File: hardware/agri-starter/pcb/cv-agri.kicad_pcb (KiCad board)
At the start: 2 copper layers, 110.2 x 87.3 mm, 54 parts, among them J1 2P 5.08mm, J2 2P 5.08mm, J3 4P 5.08mm, K1 SRD-05VDC-SL-C, M1 SIM800L, Q1 S8050, U1 ESP32-WROOM-32E (4MB), U2 AMS1117-3.3, U3 MP1584 buck (4V)

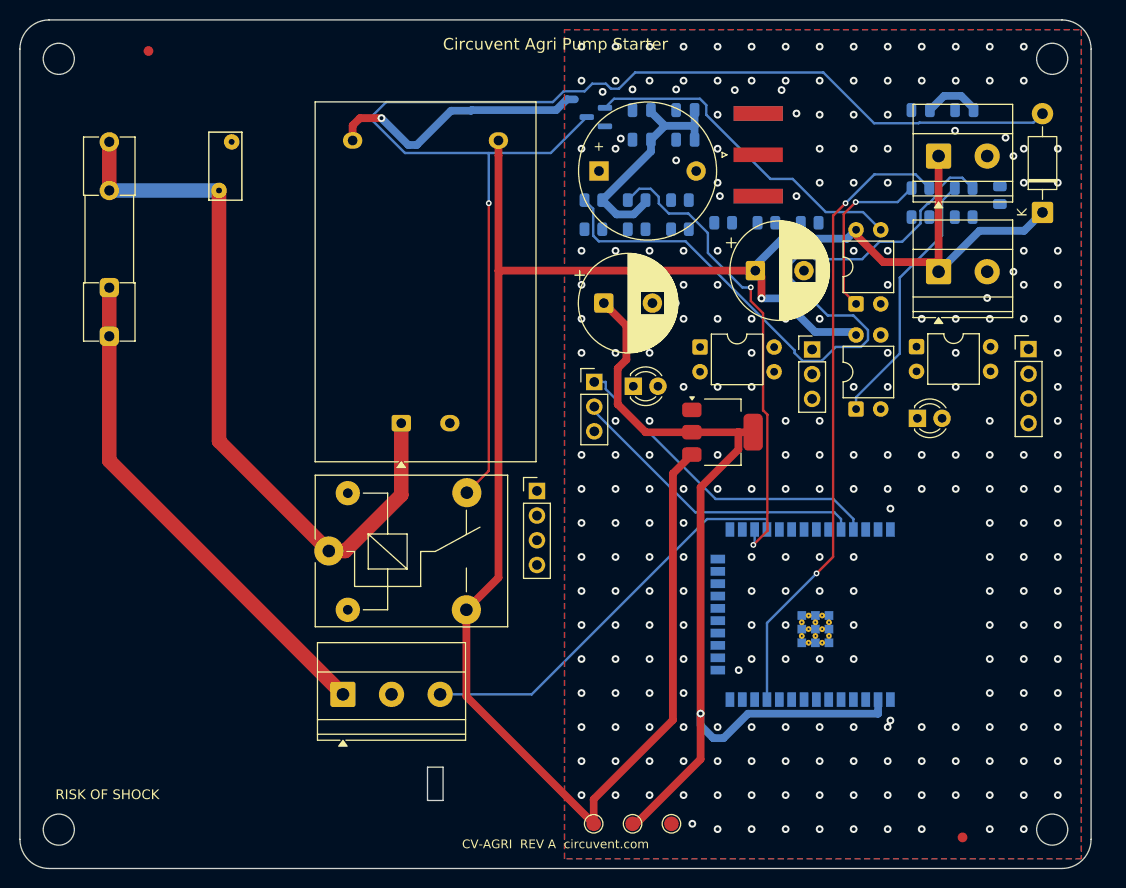
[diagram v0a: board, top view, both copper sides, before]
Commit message: hardware: fix mains isolation barrier gaps, add load-controller PCB
Adds the 13th board (ultra-compact dual-channel load controller: ESP32-C3,
opto+relay channel, MOSFET PWM channel, USB-C, AP2112K LDO, USBLC6 ESD) and
regenerates all 12 existing boards, which were stale with respect to earlier
relay-pinout and LED-polarity fixes.

The substantive change is to the mains isolation barrier. It is a keepout band
the router must not cross, deliberately cut where a component straddles it
because there the isolation is provided by the part's package. Three linked
defects made those cuts unsafe, each only visible once the previous was fixed:

1. The cut removed the barrier across the full band width for the straddling
   part's whole height, while the ISO_BRIDGE area that excuses the gap covered
   only the part itself. The router used the leftover strip beside the part to
   bring +5V within 6.99 mm of AC_N against an 8.0 mm reinforced creepage rule.
2. Straddling parts can overlap in y, so cutting per part put one part's
   keepout on another part's pads. The exempt x-ranges are now unioned per
   strip by a sweep line.
3. The rule only relaxes for items insideArea('ISO_BRIDGE'). With the hole the
   same size as the area, a track could hug the hole's edge without being
   contained in it, so the rule fired anyway and the router had no way to know.
   The hole is now the part's pad bbox + 0.3 mm, strictly inside ISO_BRIDGE at
   the footprint bbox + 0.6 mm.

The tighter hole leaves mains nets less room to reach bridge pads, so some
boards report more unconnected items. That is deliberate: those are documented
hand-routing items, whereas a creepage violation is a safety defect.

Also fixed in the generator:
- _pad_shape() derived a pad's layers from PAD::GetLayer(), which returns F.Cu
  even for pads on B.Cu. Every back-side pad became a phantom obstacle on the
  front, blocking legal paths there while hiding the real one behind. Only
  IsOnLayer() is truthful.
- Castella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
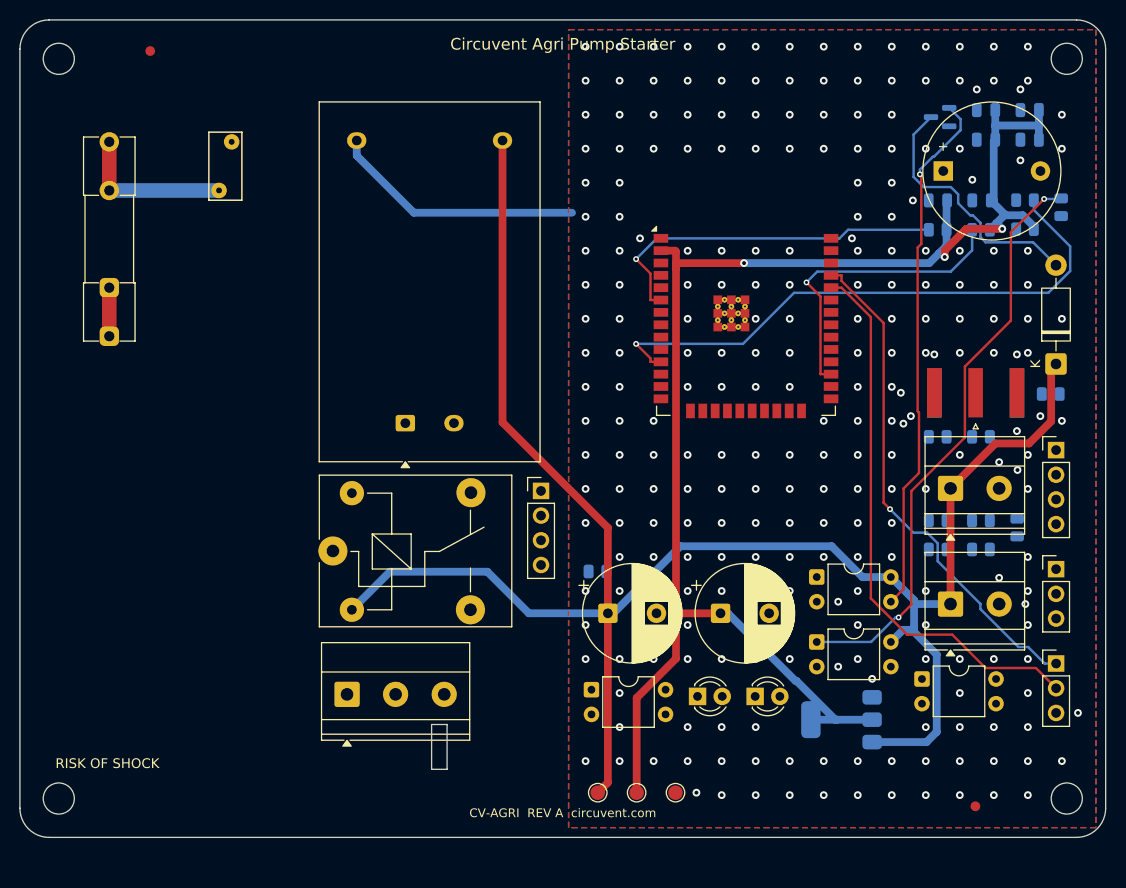
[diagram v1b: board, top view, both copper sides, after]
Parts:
- U1: moved to F.Cu
- U2: moved to B.Cu
- moved JP 55.6 mm to (206.6, 146.2)
- moved R13 48.4 mm to (198.9, 134.5)
- moved R12 48.4 mm to (194.4, 134.5)
- moved R6 43.0 mm to (206.0, 118.5)
- moved C1 38.4 mm to (160.5, 141.0)
- moved R11 37.9 mm to (202.6, 132.2), turned to 90 degrees
- moved R10 37.7 mm to (198.9, 131.5)
- moved R9 37.7 mm to (194.4, 131.5)
- moved PC4 37.0 mm to (158.8, 148.9)
- moved R14 36.2 mm to (159.4, 136.7)
- moved R5 35.6 mm to (198.9, 101.6)
- moved R4 35.6 mm to (194.4, 101.6)
- moved C2 35.4 mm to (199.4, 89.3)
- moved C3 35.4 mm to (203.9, 89.3)
- moved FB1 35.4 mm to (195.0, 95.5)
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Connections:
- K1 pad 2: PUMP_RELAY_SW -> +5V
- K1 pad 3: +5V -> PUMP_RELAY_SW
- K1 pad 4: PUMP_RELAY_COIL -> N$K1.4
- K1 pad 5: N$K1.5 -> PUMP_RELAY_COIL
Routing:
- net PUMP_RELAY_COIL: track 135.0 -> 26.7 mm, vias 1 -> 0
- net AC_L_FUSED: track 75.3 -> 16.3 mm
- net AC_L: track 51.8 -> 5.00 mm
- net SIM_TX: track 42.2 -> 0.00 mm
- net MAINS_SENSE: track 75.6 -> 37.3 mm, vias 0 -> 1
- net MAINS_SENSE_OPT: track 26.9 -> 60.5 mm, vias 0 -> 2
- net +3V3: track 124.6 -> 153.6 mm, vias 1 -> 3
- net UART_RX: track 31.5 -> 57.2 mm
- net PUMP_RELAY_DRV: track 34.9 -> 54.6 mm, vias 0 -> 1
- net UART_TX: track 34.0 -> 52.2 mm, vias 0 -> 1
- net PUMP_RELAY_OPT: track 17.9 -> 0.00 mm, vias 1 -> 0
- net SIM_RX: track 48.4 -> 31.6 mm, vias 2 -> 1
- net +5V: track 207.8 -> 197.8 mm, vias 1 -> 0
- net PUMP_RELAY: track 64.8 -> 60.1 mm, vias 2 -> 1
- net GND: track 27.8 -> 26.1 mm, vias 256 -> 254
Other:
- board size 110.2 x 87.3 mm -> 111.7 x 84.1 mm

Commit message: Release 1.10.0, and stop shipping permissions the app never uses
Cut 1.10.0 (versionCode 12) and built it: AAB 38 MB, APK 83 MB, signed with the
upload key, JS bundle embedded.

Checking the generated manifest before writing the Play listing turned up
permissions no one had asked for. Every one of them is printed on the store page
for users to read before they install:

  RECORD_AUDIO          expo-camera asks for the microphone so video can be
                        recorded with sound. This app only ever puts the camera
                        in barcode mode to read a QR label, and expo-speech is
                        output-only - it speaks, it does not listen. Left in,
                        Play lists "Microphone" against a home-control app,
                        which is alarming, unexplainable and untrue.
  SYSTEM_ALERT_WINDOW   React Native's development overlay, useless in a release
                        build and shown to users as "Display over other apps".
  READ/WRITE_EXTERNAL_STORAGE
                        Legacy storage access nothing here touches.

Stripped via android.blockedPermissions. That emits tools:node="remove", which
is a merge instruction rather than a guarantee, so it was checked against the
finished artifact with aapt2 rather than the source manifest - all four are
absent from the APK.

NEARBY_WIFI_DEVICES now carries neverForLocation. Android otherwise treats it as
location-capable, because knowing which networks are in range is enough to place
someone, and Play's data safety review treats it the same way. The app uses it
only to join a new device's setup hotspot. That flag is a promise, so the plugin
says plainly that it has to come off if scan results are ever used positionally.

What is left is defensible: location for Wi-Fi onboarding (Android requires it),
camera for the QR label, nearby-devices flagged as non-positional.

Added mobile/store/listing with the text Play asks for - title, short and full
descriptions, and what'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
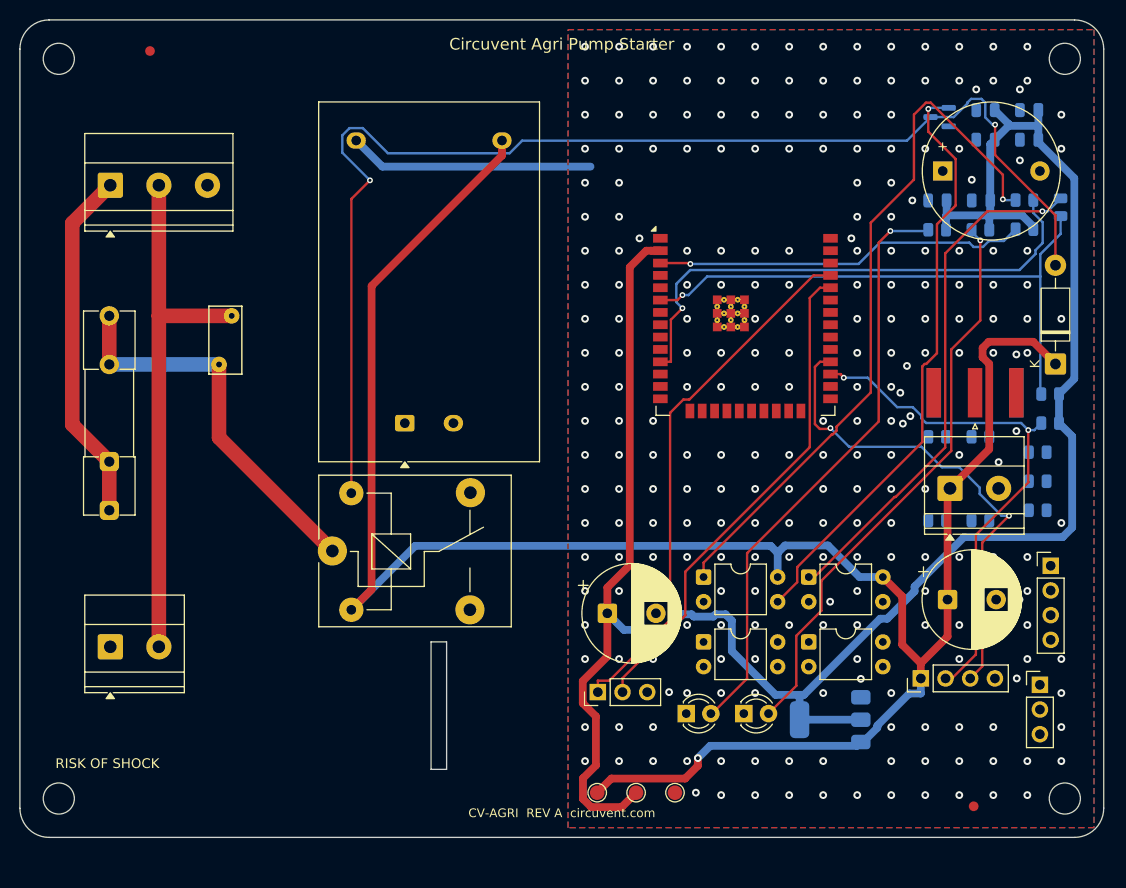
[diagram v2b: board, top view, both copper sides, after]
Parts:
- moved J2 88.0 mm to (109.3, 144.5)
- moved J1 57.8 mm to (109.3, 97.0)
- moved JP 47.2 mm to (159.5, 149.2), turned to 90 degrees
- moved M1 43.6 mm to (192.7, 147.7), turned to 90 degrees
- moved R14 39.7 mm to (198.8, 131.5)
- moved C1 35.0 mm to (195.4, 139.6)
- moved PC4 22.9 mm to (181.2, 144.0)
- moved PC3 22.8 mm to (170.3, 144.0)
- moved F1 17.9 mm to (109.2, 130.4)
- moved RV1 17.9 mm to (120.5, 115.4)
- moved SIM1 12.0 mm to (204.9, 148.4)
- moved U3 11.9 mm to (206.0, 136.2)
- moved J3 11.9 mm to (195.7, 128.2)
- moved R7 11.7 mm to (206.0, 121.5)
- moved Cs 11.6 mm to (160.4, 141.0)
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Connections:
- J1 pad 3: SIM_TX -> PE
- J2 pad 1: +5V -> PUMP_RELAY_SW
- J2 pad 2: GND -> AC_N
- LED0 pad 1: N$LED0.1 -> GND
- LED0 pad 2: N$LED0.2 -> LED0_A
- LED1 pad 1: N$LED1.1 -> GND
- LED1 pad 2: N$LED1.2 -> LED1_A
- M1 pad 2: PUMP_RELAY_SW -> SIM_RX
- M1 pad 3: SIM_RX -> SIM_TX
- M1 pad 4: AC_N -> GND
- R4 pad 2: MAINS_SENSE -> LED0_A
- R5 pad 2: SIM_RX -> LED1_A
- R6 pad 1: N$R6.1 -> +3V3
- R6 pad 2: N$R6.2 -> MAINS_SENSE
- R7 pad 1: N$R7.1 -> +3V3
- R7 pad 2: N$R7.2 -> SIM_RX
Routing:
- net PUMP_RELAY_COIL: track 26.7 -> 128.7 mm, vias 0 -> 2
- net PUMP_RELAY_OPT: track 0.00 -> 73.2 mm, vias 0 -> 1
- net LED0_A: track 0.00 -> 61.3 mm, vias 0 -> 1
- net +3V3: track 153.6 -> 214.2 mm, vias 3 -> 0
- net LED1_A: track 0.00 -> 59.2 mm, vias 0 -> 1
- net AC_N: track 0.00 -> 55.0 mm
- net SIM_TX: track 0.00 -> 50.4 mm, vias 0 -> 2
- net EN: track 0.00 -> 38.4 mm, vias 0 -> 1
- net AC_L: track 5.00 -> 36.6 mm
- net AC_L_FUSED: track 16.3 -> 40.3 mm
- net SIM_RX: track 31.6 -> 54.0 mm, vias 1 -> 2
- net MAINS_SENSE: track 37.3 -> 59.3 mm
- net +5V: track 197.8 -> 212.6 mm, vias 0 -> 1
- net PUMP_RELAY_DRV: track 54.6 -> 61.7 mm
- net MAINS_SENSE_OPT: track 60.5 -> 53.7 mm, vias 2 -> 1
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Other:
- board size 111.7 x 84.1 mm -> 111.5 x 84.1 mm
